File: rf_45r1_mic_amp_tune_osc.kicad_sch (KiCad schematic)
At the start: 0 parts

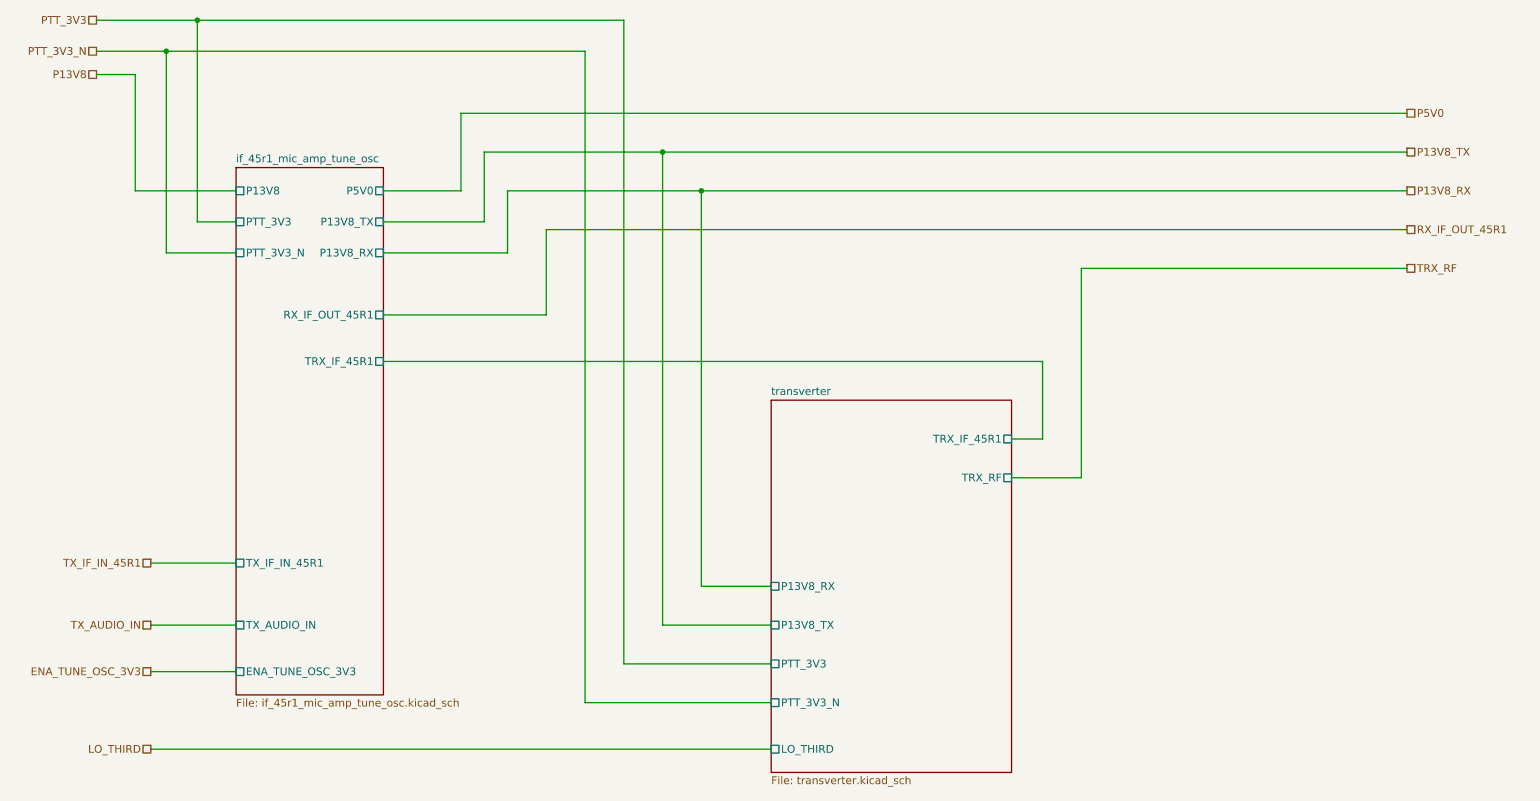
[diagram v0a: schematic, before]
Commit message: trx_mobo_concept_2_B. Change design to use a dedicated 8V supply for the 2SC3357 parts. Add S-Meter connector. Change mic connector to 3 pins and add 8V sopower supply to pin 3.
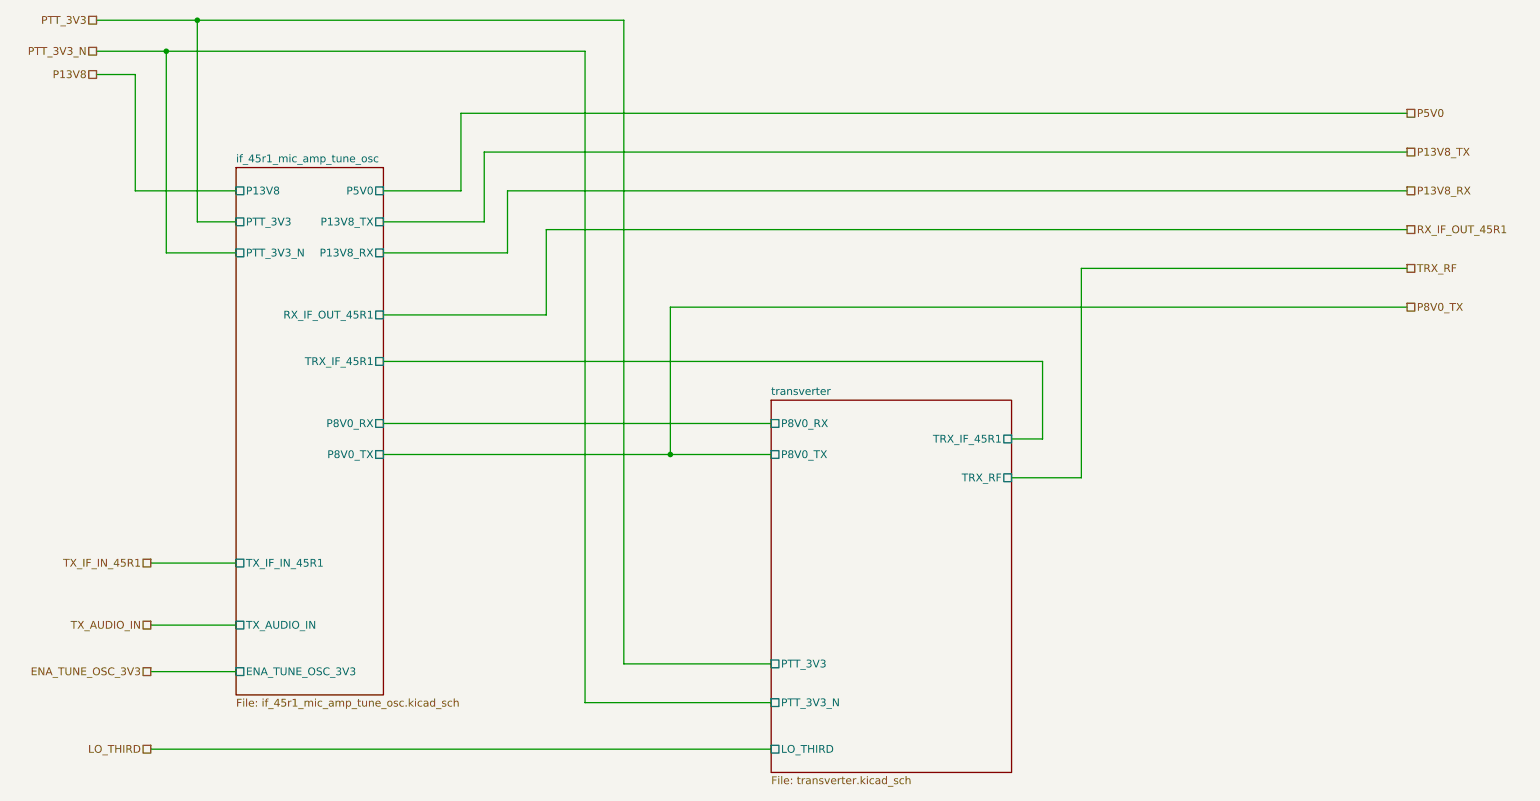
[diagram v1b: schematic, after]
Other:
- sheet if_45r1_mic_amp_tune_osc ports: added P8V0_RX, P8V0_TX; removed none
- sheet transverter ports: added P8V0_RX, P8V0_TX; removed P13V8_RX, P13V8_TX
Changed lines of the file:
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@@
   (paper "A4")
   (title_block
-    (rev "X1")
+    (rev "B")
     (company "WA6ZFT")
   )
-  (junction (at 128.27 43.18) (diameter 0) (color 0 0 0 0)
-  )
-  (junction (at 121.92 36.83) (diameter 0) (color 0 0 0 0)
-  )
   (junction (at 40.64 20.32) (diameter 0) (color 0 0 0 0)
   )
   (junction (at 45.72 15.24) (diameter 0) (color 0 0 0 0)
   )
+  (junction (at 123.19 86.36) (diameter 0) (color 0 0 0 0)
+  )
   (wire (pts (xy 102.87 49.53) (xy 243.84 49.53))
     (stroke (width 0) (type default) (color 0 0 0 0))
   )
+  (wire (pts (xy 76.2 81.28) (xy 139.7 81.28))
+    (stroke (width 0) (type default) (color 0 0 0 0))
+  )
   (wire (pts (xy 115.57 120.65) (xy 139.7 120.65))
     (stroke (width 0) (type default) (color 0 0 0 0))
@@
     (stroke (width 0) (type default) (color 0 0 0 0))
   )
-  (wire (pts (xy 121.92 36.83) (xy 92.71 36.83))
+  (wire (pts (xy 92.71 36.83) (xy 243.84 36.83))
     (stroke (width 0) (type default) (color 0 0 0 0))
   )
@@
     (stroke (width 0) (type default) (color 0 0 0 0))
   )
-  (wire (pts (xy 243.84 36.83) (xy 121.92 36.83))
-    (stroke (width 0) (type default) (color 0 0 0 0))
-  )
   (wire (pts (xy 40.64 20.32) (xy 29.21 20.32))
     (stroke (width 0) (type default) (color 0 0 0 0))
@@
     (stroke (width 0) (type default) (color 0 0 0 0))
   )
-  (wire (pts (xy 96.52 43.18) (xy 128.27 43.18))
+  (wire (pts (xy 96.52 43.18) (xy 243.84 43.18))
     (stroke (width 0) (type default) (color 0 0 0 0))
   )
@@
     (stroke (width 0) (type default) (color 0 0 0 0))
   )
-  (wire (pts (xy 139.7 114.3) (xy 121.92 114.3))
-    (stroke (width 0) (type default) (color 0 0 0 0))
-  )
   (wire (pts (xy 184.15 71.12) (xy 184.15 83.82))
     (stroke (width 0) (type default) (color 0 0 0 0))
   )
-  (wire (pts (xy 121.92 114.3) (xy 121.92 36.83))
-    (stroke (width 0) (type default) (color 0 0 0 0))
-  )
   (wire (pts (xy 45.72 15.24) (xy 29.21 15.24))
     (stroke (width 0) (type default) (color 0 0 0 0))
   )
+  (wire (pts (xy 123.19 86.36) (xy 123.19 62.23))
+    (stroke (width 0) (type default) (color 0 0 0 0))
+  )
   (wire (pts (xy 88.9 43.18) (xy 76.2 43.18))
     (stroke (width 0) (type default) (color 0 0 0 0))
@@
     (stroke (width 0) (type default) (color 0 0 0 0))
   )
-  (wire (pts (xy 139.7 107.95) (xy 128.27 107.95))
-    (stroke (width 0) (type default) (color 0 0 0 0))
-  )
-  (wire (pts (xy 128.27 107.95) (xy 128.27 43.18))
+  (wire (pts (xy 123.19 86.36) (xy 139.7 86.36))
+    (stroke (width 0) (type default) (color 0 0 0 0))
+  )
+  (wire (pts (xy 123.19 62.23) (xy 243.84 62.23))
     (stroke (width 0) (type default) (color 0 0 0 0))
   )
@@
     (stroke (width 0) (type default) (color 0 0 0 0))
   )
-  (wire (pts (xy 128.27 43.18) (xy 243.84 43.18))
+  (wire (pts (xy 76.2 86.36) (xy 123.19 86.36))
     (stroke (width 0) (type default) (color 0 0 0 0))
   )
@@
   (wire (pts (xy 52.07 53.34) (xy 40.64 53.34))
     (stroke (width 0) (type default) (color 0 0 0 0))
+  )
+  (hierarchical_label "P8V0_TX" (shape passive) (at 243.84 62.23 0)
+    (effects (font (size 1.27 1.27)) (justify left))
   )
   (hierarchical_label "RX_IF_OUT_45R1" (shape passive) (at 243.84 49.53 0)
@@
       (effects (font (size 1.27 1.27)) (justify left))
     )
-    (pin "P13V8_TX" passive (at 139.7 114.3 180)
-      (effects (font (size 1.27 1.27)) (justify left))
-    )
-    (pin "P13V8_RX" passive (at 139.7 107.95 180)
+    (pin "P8V0_RX" passive (at 139.7 81.28 180)
+      (effects (font (size 1.27 1.27)) (justify left))
+    )
+    (pin "P8V0_TX" passive (at 139.7 86.36 180)
       (effects (font (size 1.27 1.27)) (justify left))
     )
@@
       (effects (font (size 1.27 1.27)) (justify right))
     )
+    (pin "P8V0_RX" passive (at 76.2 81.28 0)
+      (effects (font (size 1.27 1.27)) (justify right))
+    )
+    (pin "P8V0_TX" passive (at 76.2 86.36 0)
+      (effects (font (size 1.27 1.27)) (justify right))
+    )
